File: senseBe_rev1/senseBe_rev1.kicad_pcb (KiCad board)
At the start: 2 copper layers, 40 x 60 mm, 52 parts, among them J1 PJ-32434_3-5mmAudioJack, P1 CONN_02X05, Q1 TSM2301, Q2 SI2302, Q3 SI2302, Q4 SI2302, Q5 SI2302, Q6 SI2302, Q7 SI2302, SW1 SW_SPST, SW2 SW_DPST, U1 MDBT42Q, U2 TSSP4056, U3 AP3403, Y1 T38 Mercury

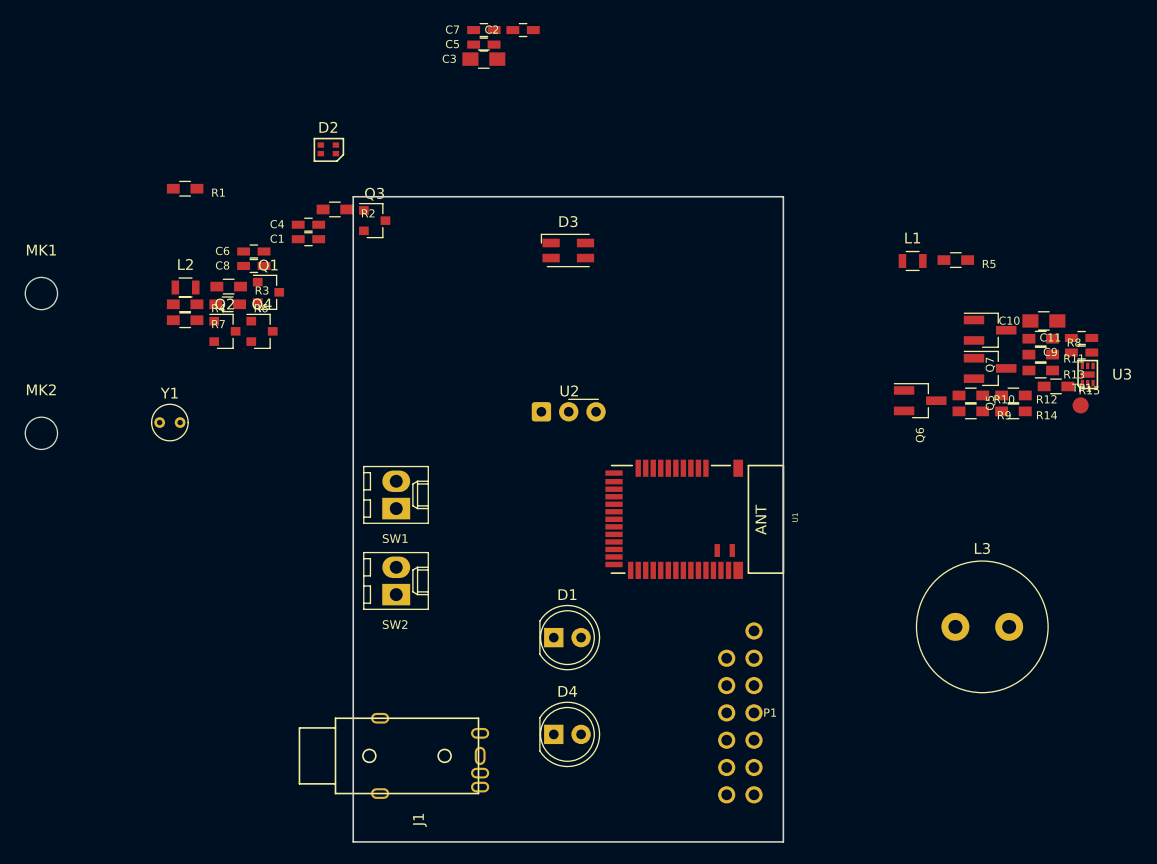
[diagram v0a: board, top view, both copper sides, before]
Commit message: Completes Schematic and PCB Design.
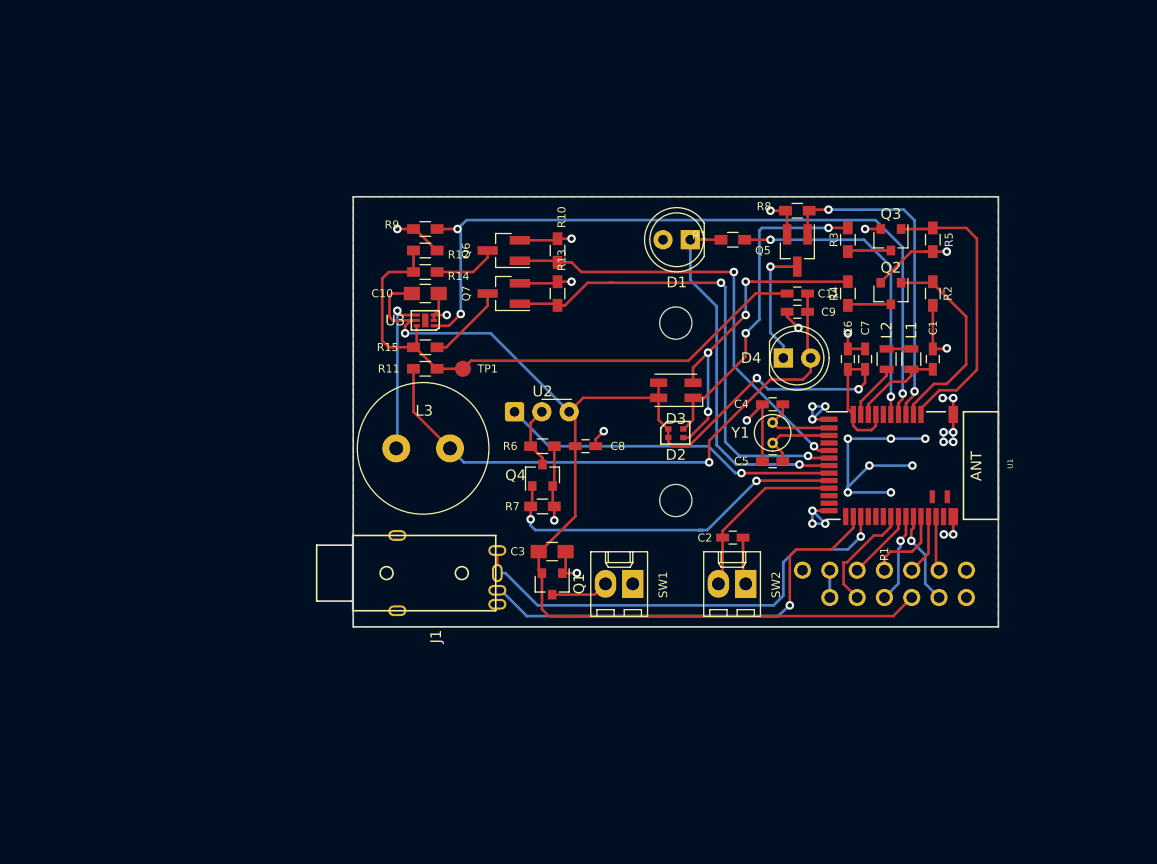
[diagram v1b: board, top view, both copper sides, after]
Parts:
- moved L2 65.5 mm to (49.6, 15.1), turned to 270 degrees
- moved Q2 62.0 mm to (50.0, 9.00), turned to 270 degrees
- moved U3 61.8 mm to (6.70, 11.5), turned to 90 degrees
- moved R4 61.6 mm to (46.0, 9.00), turned to 90 degrees
- moved MK2 59.3 mm to (30.0, 28.2)
- moved C1 59.1 mm to (53.9, 15.1), turned to 270 degrees
- moved MK1 59.1 mm to (30.0, 11.8)
- moved R15 58.8 mm to (6.70, 14.0)
- moved R3 57.7 mm to (46.0, 4.00), turned to 90 degrees
- moved C10 57.6 mm to (6.70, 9.00)
- moved TP1 57.5 mm to (10.2, 16.0)
- moved R11 57.3 mm to (6.70, 16.0)
- moved Y1 57.0 mm to (39.0, 21.0), turned to 270 degrees
- moved R12 56.3 mm to (6.70, 5.00)
- moved R14 56.2 mm to (6.70, 7.00)
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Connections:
- Q5 pad 1: /Sheet5C63BFE7/IR_LED_EN -> /IR_LED_EN
- Q6 pad 1: /Sheet5C63BFE7/PWR1 -> /PWR1
- Q7 pad 1: /Sheet5C63BFE7/PWR2 -> /PWR2
- R10 pad 1: /Sheet5C63BFE7/PWR1 -> /PWR1
- R13 pad 1: /Sheet5C63BFE7/PWR2 -> /PWR2
- R8 pad 1: /Sheet5C63BFE7/IR_LED_EN -> /IR_LED_EN
- R9 pad 1: /Sheet5C63BFE7/REG_EN -> /REG_EN
- U1 pad 16: (no net) -> /PWR1
- U1 pad 17: (no net) -> /PWR2
- U1 pad 4: (no net) -> /IR_LED_EN
- U1 pad 5: (no net) -> /REG_EN
- U3 pad 1: /Sheet5C63BFE7/REG_EN -> /REG_EN
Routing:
- net VDD: track 0.00 -> 131.1 mm, vias 0 -> 3
- net GND: track 0.00 -> 89.1 mm, vias 0 -> 28
- net /REG_EN: track 0.00 -> 71.4 mm, vias 0 -> 3
- net /Sheet5C63BFE7/VLED: track 0.00 -> 54.9 mm, vias 0 -> 1
- net Net-(C11-Pad2): track 0.00 -> 54.7 mm
- net /PWR2: track 0.00 -> 45.2 mm, vias 0 -> 2
- net /TRIGGER: track 0.00 -> 43.5 mm, vias 0 -> 1
- net /FOCUS: track 0.00 -> 41.2 mm, vias 0 -> 1
- net /PWR1: track 0.00 -> 41.2 mm, vias 0 -> 2
- net /LIGHT_SENSE: track 0.00 -> 34.2 mm, vias 0 -> 1
- net /RX_EN: track 0.00 -> 34.0 mm, vias 0 -> 2
- net /RX_OUT: track 0.00 -> 31.6 mm, vias 0 -> 1
- net /IR_LED_EN: track 0.00 -> 30.9 mm, vias 0 -> 2
- net Net-(D2-Pad2): track 0.00 -> 30.4 mm, vias 0 -> 2
- net Net-(D2-Pad4): track 0.00 -> 30.1 mm, vias 0 -> 4
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- added copper zone on B.Cu, net GND
- added copper zone on F.Cu, net GND
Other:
- board size 40 x 60 mm -> 60 x 40 mm

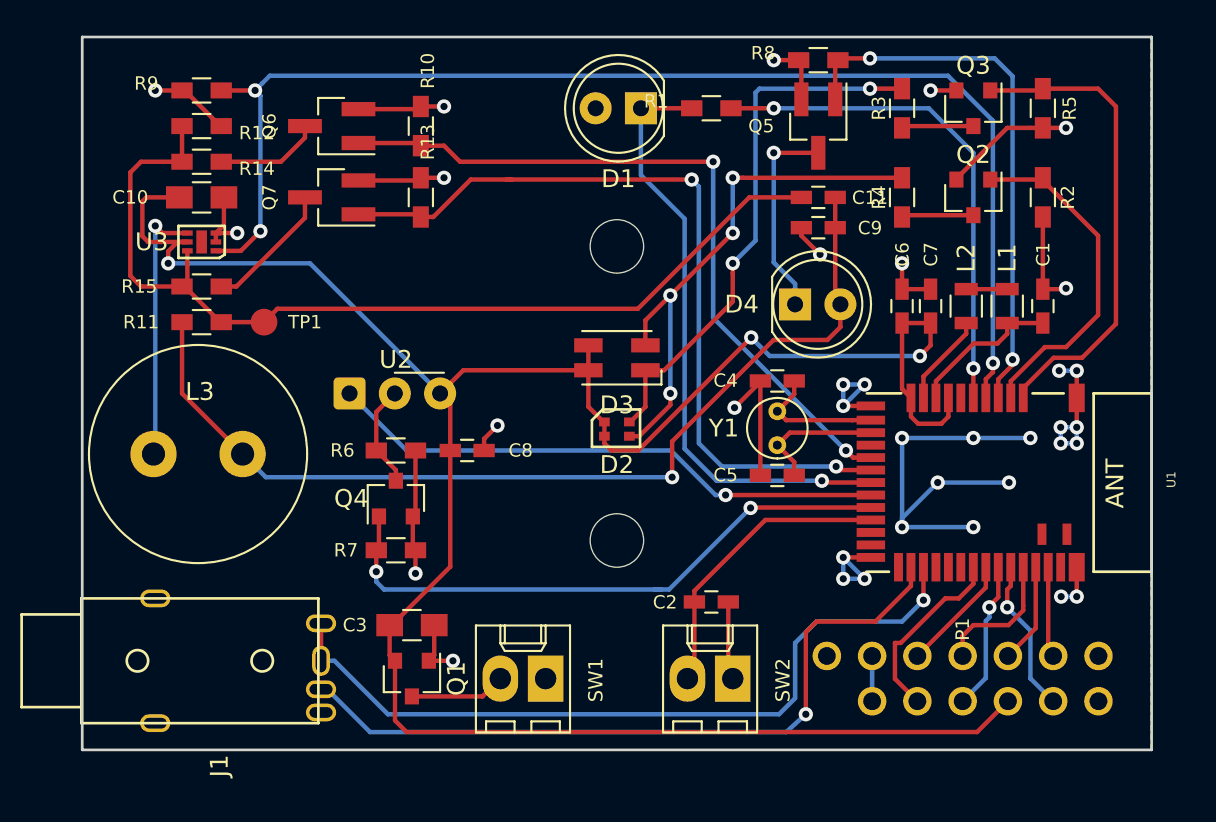
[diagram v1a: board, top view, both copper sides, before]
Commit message: Ref designators, keepouts, pour gnd, switch gnd corrected. Dual LED overlapping now.
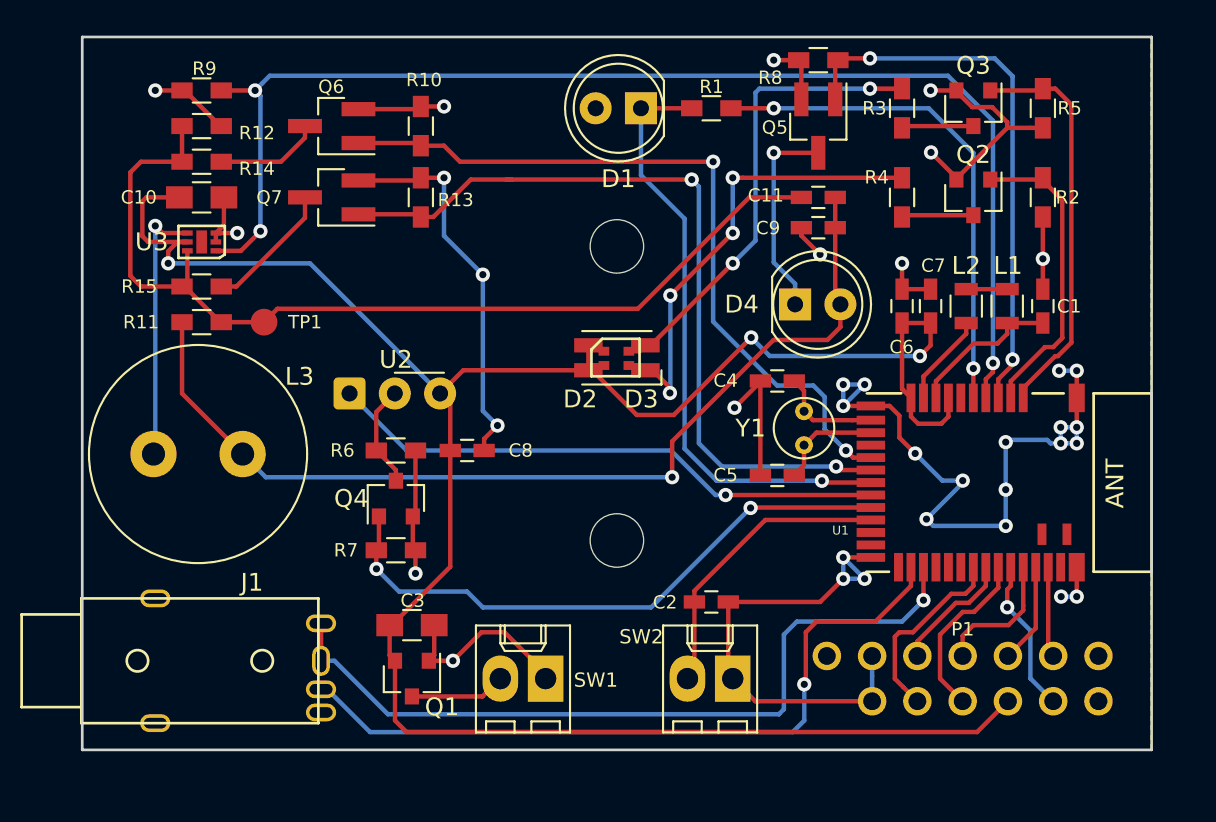
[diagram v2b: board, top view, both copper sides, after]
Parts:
- moved D2 3.97 mm to (30.0, 18.0)
- moved Y1 1.50 mm to (40.5, 21.0)
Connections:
- D3 pad 2: Net-(D2-Pad2) -> Net-(D2-Pad4)
- D3 pad 4: Net-(D2-Pad4) -> Net-(D2-Pad2)
- SW1 pad 1: (no net) -> GND
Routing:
- net GND: track 89.1 -> 153.3 mm, vias 28 -> 35
- net (no net): track 23.5 -> 0.00 mm, vias 7 -> 0
- net /LED_GREEN: track 26.9 -> 22.6 mm
- net Net-(D2-Pad2): track 30.4 -> 26.3 mm
- net Net-(D2-Pad4): track 30.1 -> 26.2 mm
- net /LED_RED: track 19.3 -> 17.3 mm
- net /LFCLK_XL2: track 7.63 -> 5.97 mm
- net /LFCLK_XL1: track 7.55 -> 5.88 mm
- net VDD: track 131.1 -> 129.5 mm
- net /GPIO1: track 8.35 -> 9.77 mm, vias 1 -> 0
- net /PWR1: track 41.2 -> 42.4 mm
- net /TRIGGER: track 43.5 -> 44.1 mm
